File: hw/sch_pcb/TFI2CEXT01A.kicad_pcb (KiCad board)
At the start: 2 copper layers, 25 x 15 mm, 26 parts, among them J1 SM04B-GHS-TB, J2 SM04B-GHS-TB, J3 SM04B-GHS-TB, J4 SM04B-GHS-TB, M1 HOLE, M2 HOLE, M2 M3, M3 HOLE, M4 HOLE, M5 HOLE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

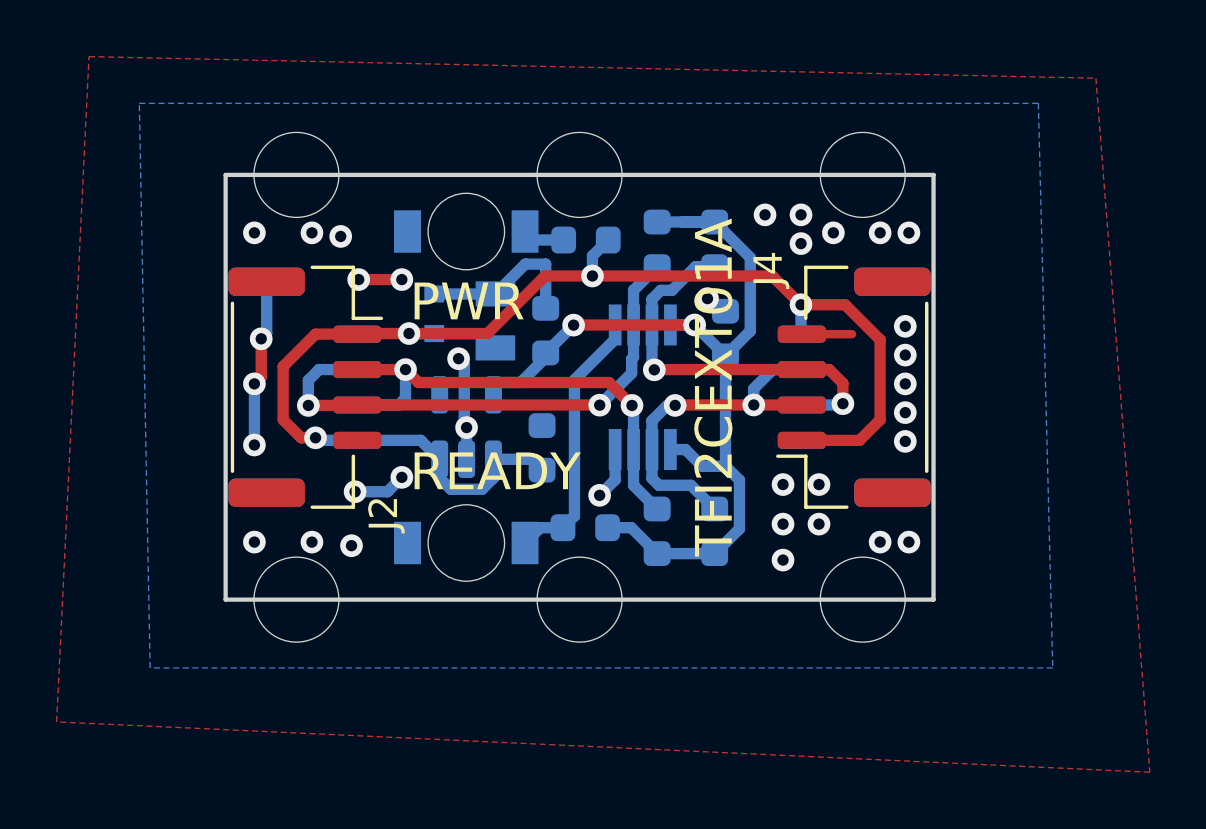
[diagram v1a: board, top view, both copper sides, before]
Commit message: Improved Slave and Master side marking. #6.
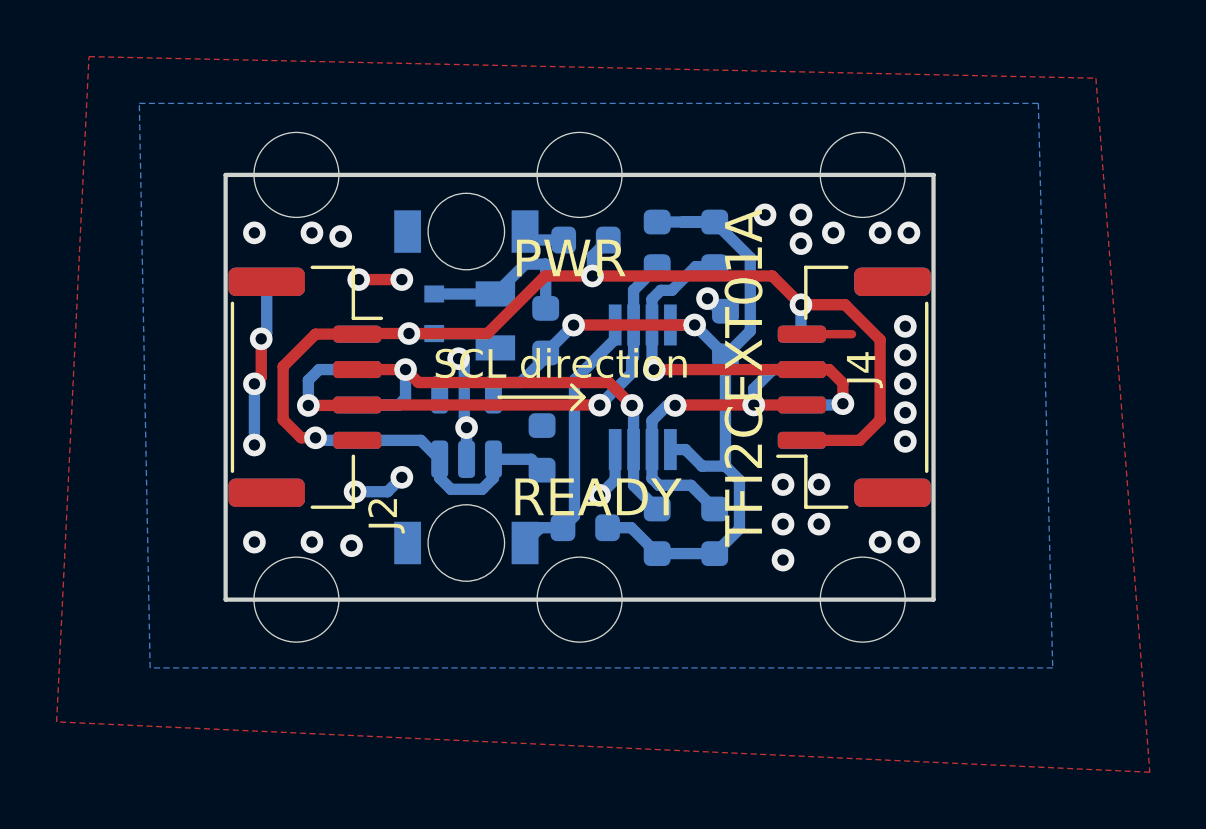
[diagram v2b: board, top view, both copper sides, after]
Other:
- board text added: "Master"
- board text added: "SCL direction"
- board text added: "Slaves"
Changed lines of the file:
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@@
-(kicad_pcb (version 20210228) (generator pcbnew)
+(kicad_pcb (version 20210424) (generator pcbnew)
   (general
     (thickness 1.6)
@@
     (property "UST_id" "")
     (attr smd)
-    (fp_text reference "J4" (at 4.184 -3.023 90) (layer "F.SilkS")
+    (fp_text reference "J4" (at 0.6788 0.279 90) (layer "F.SilkS")
       (effects (font (size 1 1) (thickness 0.15)))
     )
@@
     (property "Sheetname" "")
     (attr smd)
-    (fp_text reference "U2" (at 0 2.5 270) (layer "B.SilkS")
+    (fp_text reference "U2" (at -0.1086 -2.3114 270) (layer "B.SilkS")
       (effects (font (size 1 1) (thickness 0.15)) (justify mirror))
     )
@@
     (property "UST_id" "")
     (attr smd)
-    (fp_text reference "C3" (at 0 1.43 270) (layer "B.SilkS")
+    (fp_text reference "C3" (at 1.9559 0.0762) (layer "B.SilkS")
       (effects (font (size 1 1) (thickness 0.15)) (justify mirror))
     )
@@
     (property "UST_id" "")
     (attr smd)
-    (fp_text reference "J3" (at -4.057 2.896 -90) (layer "B.SilkS")
+    (fp_text reference "J3" (at -0.6026 -0.4822 -90) (layer "B.SilkS")
       (effects (font (size 1 1) (thickness 0.15)) (justify mirror))
     )
@@
     (property "UST_id" "")
     (attr smd)
-    (fp_text reference "C4" (at 0 1.43 270) (layer "B.SilkS")
+    (fp_text reference "C4" (at -1.4224 -1.4224 270) (layer "B.SilkS")
       (effects (font (size 1 1) (thickness 0.15)) (justify mirror))
     )
@@
     )
   )
+  (gr_line (start 12.6492 -7.1374) (end 12.2174 -6.7056) (layer "F.SilkS") (width 0.12))
+  (gr_line (start 12.6492 -7.1501) (end 12.2174 -7.5819) (layer "F.SilkS") (width 0.12))
+  (gr_line (start 9.652 -7.1501) (end 12.6492 -7.1501) (layer "F.SilkS") (width 0.12))
   (gr_line (start 0 -15) (end 25 -15) (layer "Edge.Cuts") (width 0.15))
   (gr_line locked (start 25 -15) (end 25 0) (layer "Edge.Cuts") (width 0.15))
   (gr_line locked (start 0 -15) (end 0 0) (layer "Edge.Cuts") (width 0.15))
   (gr_line locked (start 0 0) (end 25 0) (layer "Edge.Cuts") (width 0.15))
-  (gr_text "PWR" (at 6.5 -10.5) (layer "F.SilkS")
+  (gr_text "Slaves" (at 18.7452 -7.366 90) (layer "B.SilkS")
+    (effects (font (size 1 1) (thickness 0.15)) (justify mirror))
+  )
+  (gr_text "Master" (at 6.477 -7.493 90) (layer "B.SilkS")
+    (effects (font (size 1 1) (thickness 0.15)) (justify mirror))
+  )
+  (gr_text "PWR" (at 10.1092 -12.0142) (layer "F.SilkS")
     (effects (font (size 1.3 1.3) (thickness 0.3)) (justify left))
   )
-  (gr_text "READY" (at 6.5 -4.5) (layer "F.SilkS")
+  (gr_text "READY" (at 10.0584 -3.5814) (layer "F.SilkS")
     (effects (font (size 1.3 1.3) (thickness 0.3)) (justify left))
   )
-  (gr_text "TFI2CEXT01A" (at 17.272 -7.5 90) (layer "F.SilkS")
+  (gr_text "SCL direction" (at 11.8618 -8.3058) (layer "F.SilkS")
+    (effects (font (size 1 1) (thickness 0.15)))
+  )
+  (gr_text "TFI2CEXT01A" (at 18.3388 -7.8486 90) (layer "F.SilkS")
     (effects (font (size 1.3 1.3) (thickness 0.3)))
   )
@@
     )
   )
+  (group "" (id f87b307e-44da-44bf-9db3-5d39deda4151)
+    (members
+      0d58b41b-41cb-4e8c-ae00-b5fe566de42a
+      d71e15a3-238d-4ae1-8d4a-fe0e33b45e65
+      daa6abe2-729d-4cb8-8e90-cf037f3eb55c
+    )
+  )
